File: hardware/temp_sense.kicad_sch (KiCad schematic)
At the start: 0 parts

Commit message: temperature sensing initial
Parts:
- added C1, C2, C3, C4, C5, C6, C7, C8: 100uF, symbol Device:C
- added J1, J2, J3, J4, J5, J6, J7, J8: Conn_01x02_Pin, symbol Connector:Conn_01x02_Pin
- added R1, R12, R13, R14, R15, R2, R3, R4: 1k, symbol Device:R
- added R10, R20, R21, R9: 56k, symbol Device:R
- added R11, R22: 200k, symbol Device:R
- added R16, R5: 100k, symbol Device:R
- added R17, R6: RVar, symbol Device:R_Variable
- added R18, R19, R7, R8: 10k, symbol Device:R
- added RTD1, RTD2, RTD3, RTD4, RTD5, RTD6, RTD7, RTD8: PT100, symbol Device:R
- added U2, U4: CD4052B, symbol Analog_Switch:CD4052B
- added U3, U5: LM324, symbol Amplifier_Operational:LM324
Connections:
- new net: C5.1, J5.1 (Pin_1), R12.2, RTD5.1, U4.11 (X3)
- new net: C2.1, J2.1 (Pin_1), R2.2, RTD2.1, U2.15 (X2)
- new net: R7.1, U3.1, U3.2 (-)
- new net: R5.2, R6.1, U3.3 (+)
- new net: C8.1, J8.1 (Pin_1), R15.2, RTD8.1, U4.12 (X0)
- new net: C3.1, J3.1 (Pin_1), R3.2, RTD3.1, U2.14 (X1)
- new net: C6.1, J6.1 (Pin_1), R13.2, RTD6.1, U4.15 (X2)
- new net: R8.2, R9.2, U3.9 (-)
- new net: R16.2, R17.1, U5.3 (+)
- new net: U4.13 (X), U5.5 (+)
- new net: C7.1, J7.1 (Pin_1), R14.2, RTD7.1, U4.14 (X1)
- new net: R18.1, U5.1, U5.2 (-)
- new net: R18.2, R21.2, U5.10 (+)
- new net: C1.1, J1.1 (Pin_1), R1.2, RTD1.1, U2.11 (X3)
- new net: R19.1, U5.6 (-), U5.7
- new net: R19.2, R20.2, U5.9 (-)
- new net: U2.13 (X), U3.5 (+)
- new net: R8.1, U3.6 (-), U3.7
- new net: C4.1, J4.1 (Pin_1), R4.2, RTD4.1, U2.12 (X0)
- new net: R21.1, R22.2, U5.8
- new net: R10.2, R7.2, U3.10 (+)
- new net: R10.1, R11.2, U3.8
- new net GND: C1.2, C2.2, C3.2, C4.2, C5.2, C6.2, C7.2, C8.2, J1.2 (Pin_2), J2.2 (Pin_2), J3.2 (Pin_2), J4.2 (Pin_2), J5.2 (Pin_2), J6.2 (Pin_2), J7.2 (Pin_2), J8.2 (Pin_2), R17.2, R20.1, R6.2, R9.1, RTD1.2, RTD2.2, RTD3.2, RTD4.2, RTD5.2, RTD6.2, RTD7.2, RTD8.2, U2.6 (INH), U2.7 (VEE), U2.8 (VSS), U3.11 (V-), U4.6 (INH), U4.7 (VEE), U4.8 (VSS), U5.11 (V-)
- new net VCC: R1.1, R12.1, R13.1, R14.1, R15.1, R16.1, R2.1, R3.1, R4.1, R5.1, U2.16 (VDD), U3.4 (V+), U4.16 (VDD), U5.4 (V+)
- no-connect marks 0 -> 10

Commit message: sensing schematics
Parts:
- R1, R12, R13, R14, R15, R2, R3, R4: value 1k -> 10k
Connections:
- net VCC: no longer R1.1, R12.1, R13.1, R14.1, R15.1, R16.1, R2.1, R3.1, R4.1, U2.16 (VDD), U4.16 (VDD), U5.4 (V+)
- new net +5V: R1.1, R12.1, R13.1, R14.1, R15.1, R16.1, R2.1, R3.1, R4.1, U2.16 (VDD), U4.16 (VDD), U5.4 (V+)

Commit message: R0.0.3 Correct Voltage measurement frequency and divider
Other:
- title: [BOARD NAME] -> Discharger Main Board
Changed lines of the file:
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@@
 	(paper "B")
 	(title_block
-		(title "[BOARD NAME]")
+		(title "Discharger Main Board")
 		(date "[DATE]")
-		(rev "[REVISION]")
+		(rev "0.0.3")
 		(company "Formula Slug")
 	)

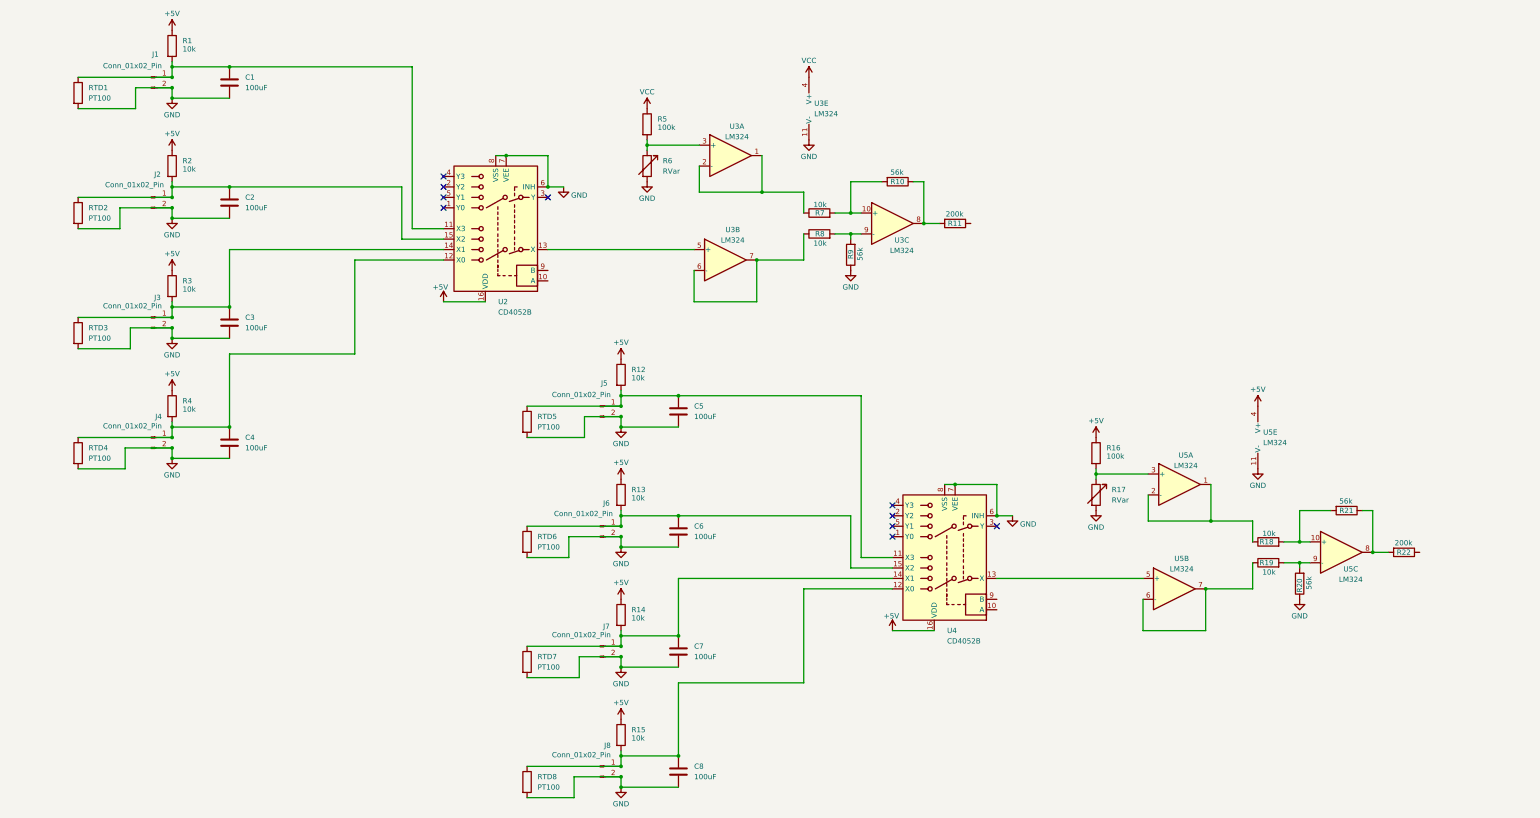
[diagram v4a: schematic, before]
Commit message: new sensor changes, need to still add low pass for voltage
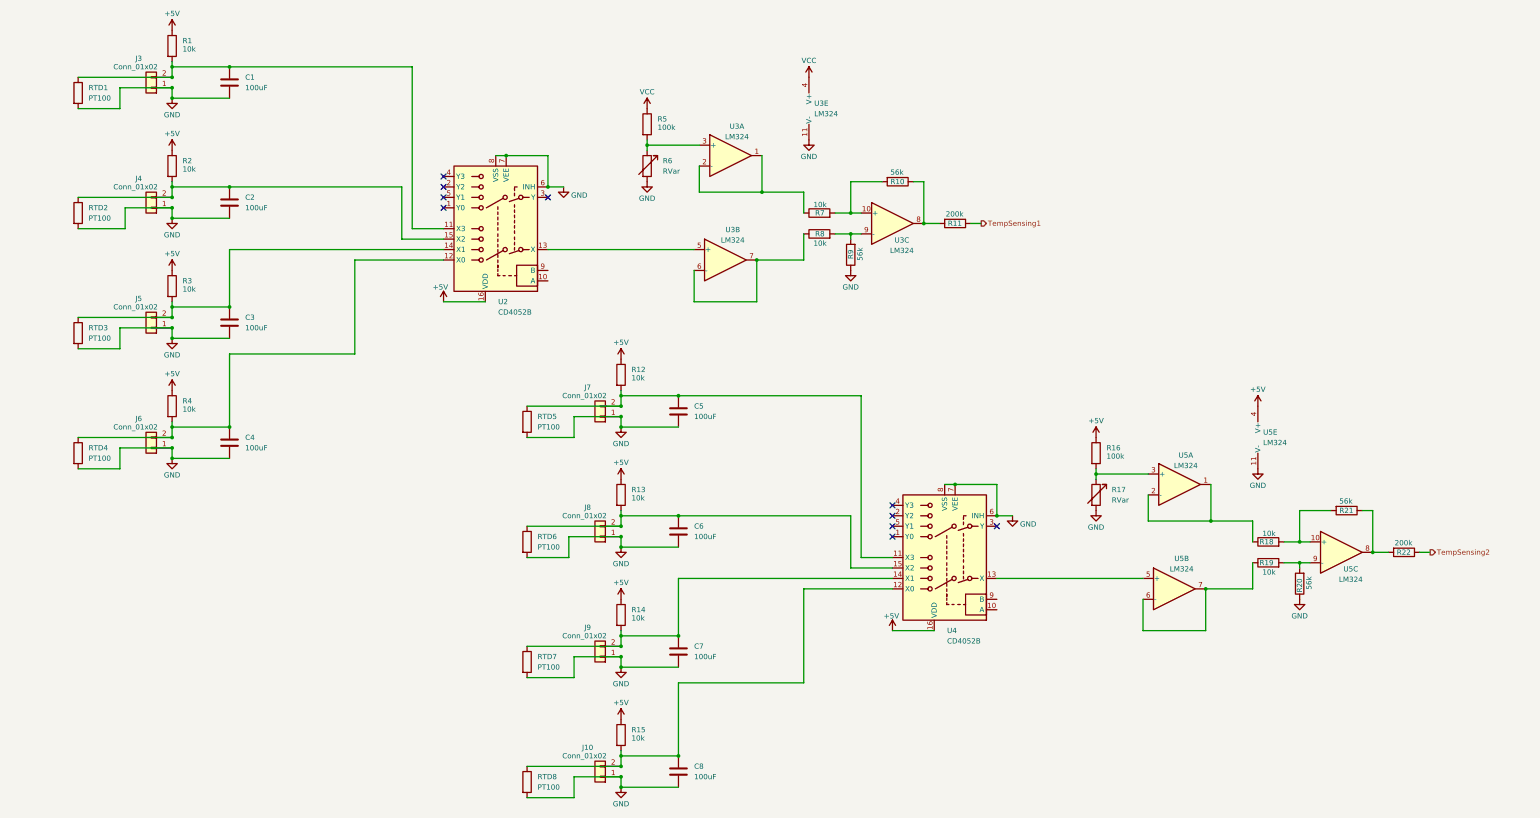
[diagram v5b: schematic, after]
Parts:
- removed J1, J2, J3, J4, J5, J6, J7, J8: Conn_01x02_Pin, symbol Connector:Conn_01x02_Pin
- added J10, J3, J4, J5, J6, J7, J8, J9: Conn_01x02, symbol Connector_Generic:Conn_01x02
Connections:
- net GND: now also J10.1 (Pin_1), J3.1 (Pin_1), J4.1 (Pin_1), J5.1 (Pin_1), J6.1 (Pin_1), J7.1 (Pin_1), J8.1 (Pin_1), J9.1 (Pin_1)
- net at C5.1, R12.2, RTD5.1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: now also J7.2 (Pin_2)
- net at C2.1, R2.2, RTD2.1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: now also J4.2 (Pin_2)
- net at C8.1, R15.2, RTD8.1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: now also J10.2 (Pin_2)
- net at C3.1, R3.2, RTD3.1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: now also J5.2 (Pin_2)
- net at C6.1, R13.2, RTD6.1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: now also J8.2 (Pin_2)
- net at C7.1, R14.2, RTD7.1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: now also J9.2 (Pin_2)
- net at C1.1, R1.2, RTD1.1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: now also J3.2 (Pin_2)
- net at C4.1, R4.2, RTD4.1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: now also J6.2 (Pin_2)
- net TempSensing1: now reaches R11.1
- net TempSensing2: now reaches R22.1

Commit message: adding connectors
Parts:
- removed J10, J3, J4, J5, J6, J7, J8, J9: Conn_01x02, symbol Connector_Generic:Conn_01x02
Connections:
- net Temp5_1: now reaches C5.1, R12.2, RTD5.1, U4.11 (X3)
- net Temp2_1: now reaches C2.1, R2.2, RTD2.1, U2.15 (X2)
- net Temp8_1: now reaches C8.1, R15.2, RTD8.1, U4.12 (X0)
- net Temp3_1: now reaches C3.1, R3.2, RTD3.1, U2.14 (X1)
- net Temp6_1: now reaches C6.1, R13.2, RTD6.1, U4.15 (X2)
- net Temp7_1: now reaches C7.1, R14.2, RTD7.1, U4.14 (X1)
- net Temp1_1: now reaches C1.1, R1.2, RTD1.1, U2.11 (X3)
- net Temp4_1: now reaches C4.1, R4.2, RTD4.1, U2.12 (X0)
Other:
- moved on the sheet: RTD1, RTD2, RTD3, RTD4, RTD5, RTD6, RTD7, RTD8

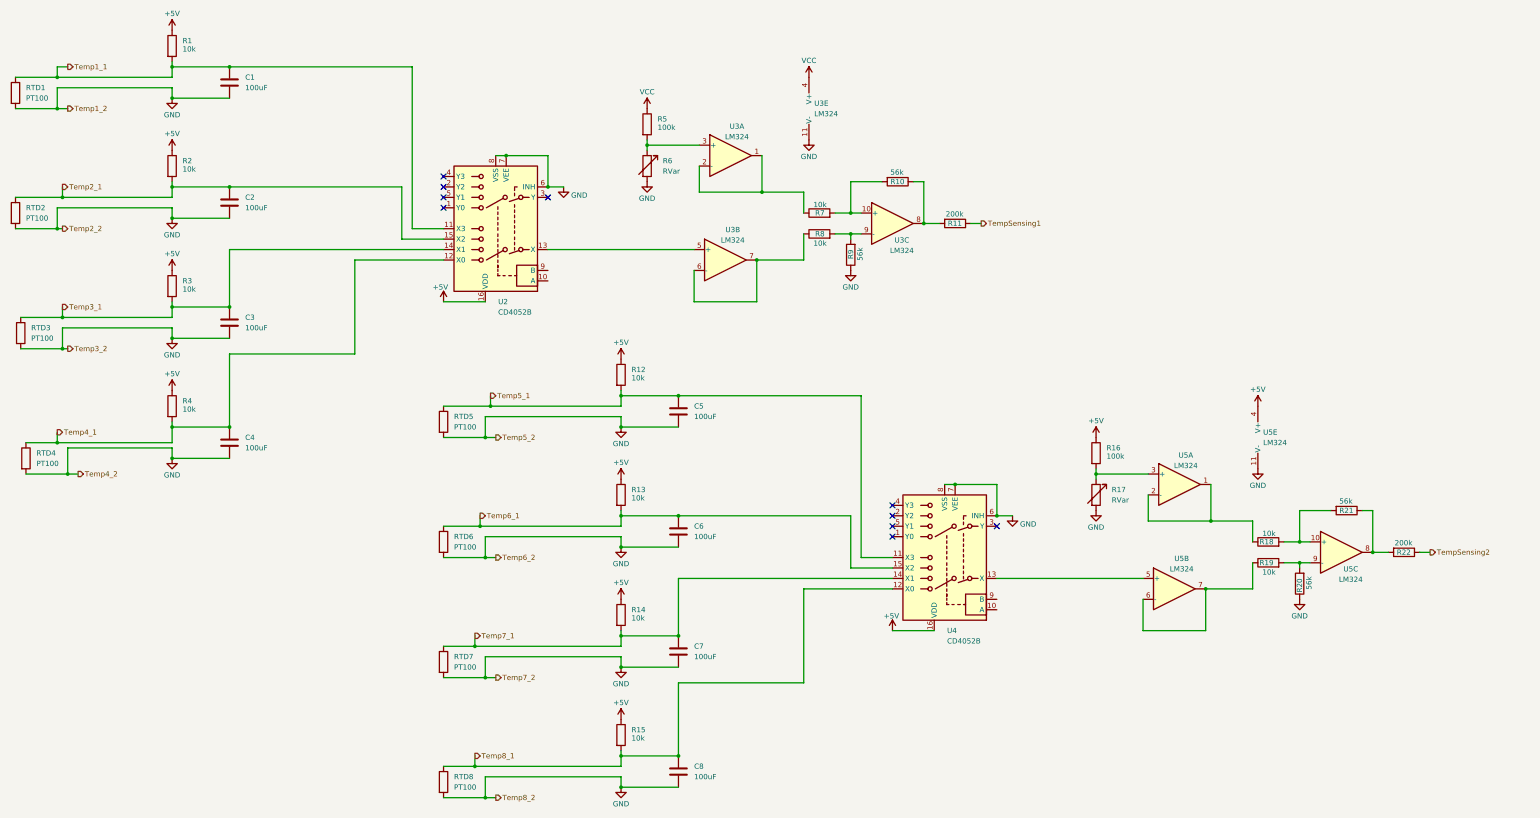
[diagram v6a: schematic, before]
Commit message: changes to sensing and footprints added
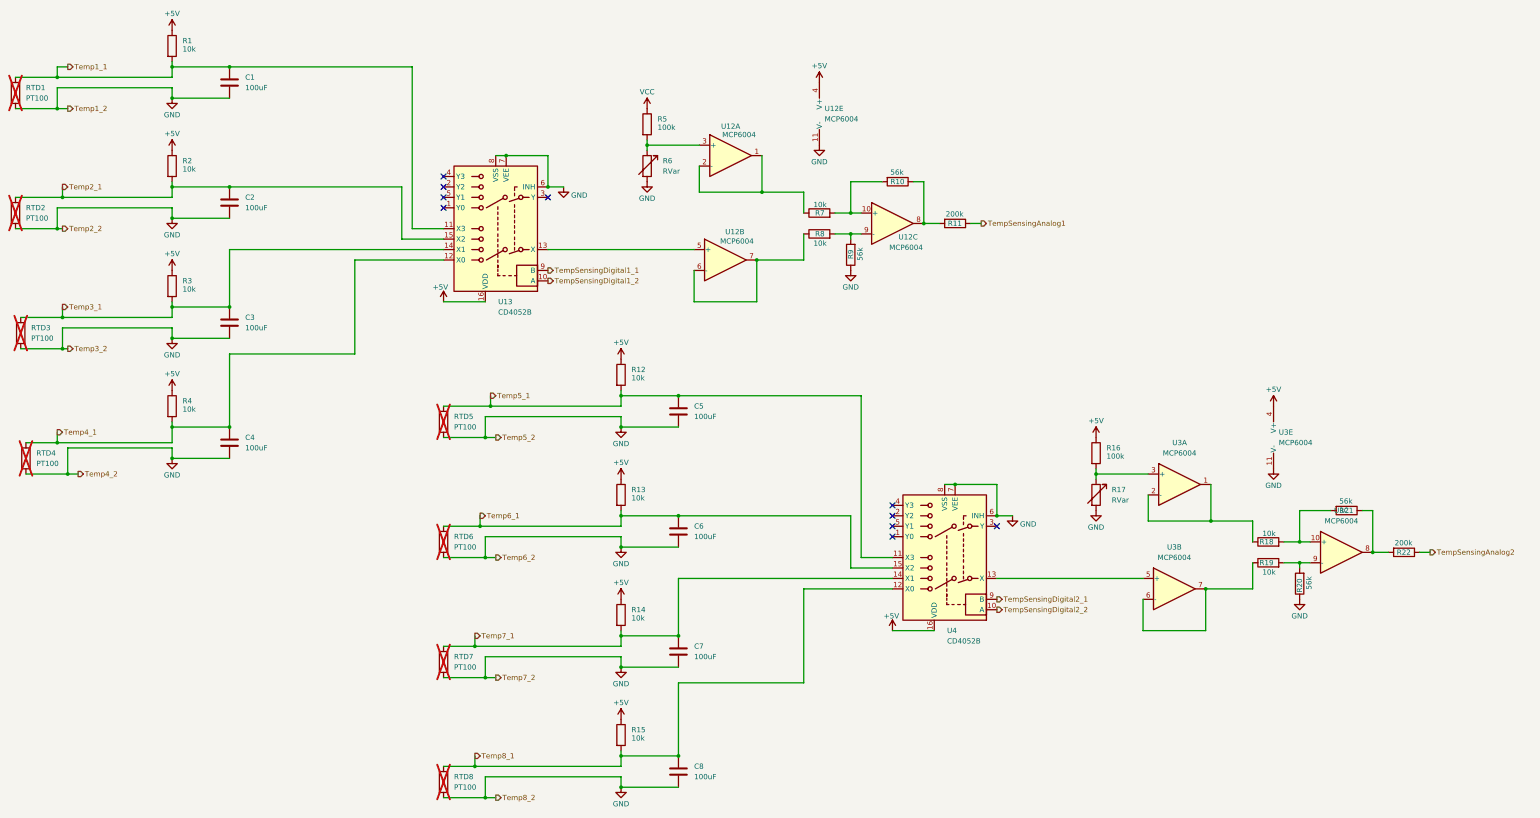
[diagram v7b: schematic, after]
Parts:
- removed U2: CD4052B, symbol Analog_Switch:CD4052B
- removed U3, U5: LM324, symbol Amplifier_Operational:LM324
- added U12, U3: MCP6004, Package_SO:SOIC-14_3.9x8.7mm_P1.27mm, symbol Amplifier_Operational:MCP6004
- added U13: CD4052B, symbol Analog_Switch:CD4052B
- C1, C2, C3, C4, C5, C6, C7, C8: footprint (none) -> Capacitor_SMD:C_0805_2012Metric_Pad1.18x1.45mm_HandSolder
- R1, R10, R11, R12, R13, R14, R15, R16, R18, R19, R2, R20, R21, R22, R3, R4, R5, R7, R8, R9: footprint (none) -> Resistor_SMD:R_0805_2012Metric_Pad1.20x1.40mm_HandSolder
- RTD1, RTD2, RTD3, RTD4, RTD5, RTD6, RTD7, RTD8: now not fitted
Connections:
- net +5V: now also U12.4 (V+), U13.16 (VDD), U3.4 (V+)
- net GND: now also U12.11 (V-), U13.6 (INH), U13.7 (VEE), U13.8 (VSS), U3.11 (V-)
- net Temp1_1: now also U13.11 (X3)
- net Temp2_1: now also U13.15 (X2)
- net Temp3_1: now also U13.14 (X1)
- net Temp4_1: now also U13.12 (X0)
- net at R7.1: now also U12.1, U12.2 (-)
- net at R5.2, R6.1: now also U12.3 (+)
- net at R8.2, R9.2: now also U12.9 (-)
- net at R16.2, R17.1: now also U3.3 (+)
- net TempSensingDigital2_2: now reaches U4.10 (A)
- net at U4.13 (X): now also U3.5 (+)
- net TempSensingDigital2_1: now reaches U4.9 (B)
- net at R18.1: now also U3.1, U3.2 (-)
- net at R18.2, R21.2: now also U3.10 (+)
- net at R19.1: now also U3.6 (-), U3.7
- net at R19.2, R20.2: now also U3.9 (-)
- net at R8.1: now also U12.6 (-), U12.7
- net at R21.1, R22.2: now also U3.8
- net at R10.2, R7.2: now also U12.10 (+)
- net at R10.1, R11.2: now also U12.8
- net TempSensing1 renamed TempSensingAnalog1
- net TempSensing2 renamed TempSensingAnalog2
- new net: U12.5 (+), U13.13 (X)
- new net TempSensingDigital1_1: U13.9 (B)
- new net TempSensingDigital1_2: U13.10 (A)
